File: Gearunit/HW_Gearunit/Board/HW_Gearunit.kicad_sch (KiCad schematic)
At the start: 37 parts, among them J1 XB-PJ-1837, J2 XB-PJ-1837, Q2 DMC2400UV, Q3 DMC2400UV, U11 LSM6DS3, U3 SIT1050TK, U4 AS5600-ASOT, U5 AS5600-ASOT, U6 CD4052B

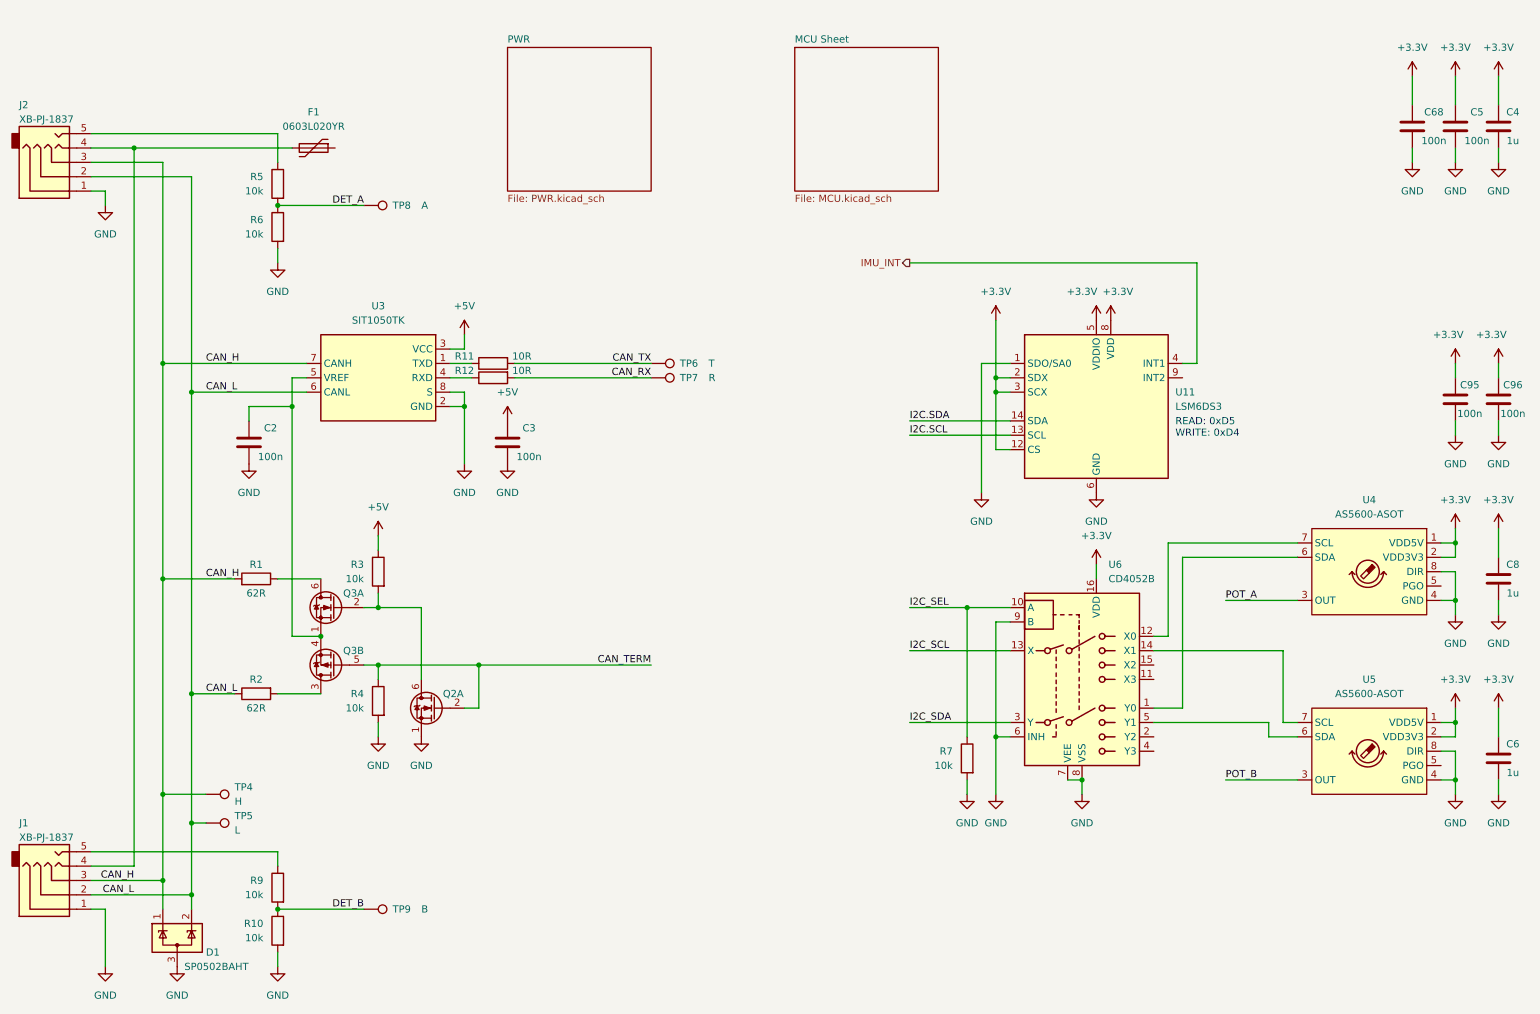
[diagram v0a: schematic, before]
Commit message: Gearunit updates, Readme updated
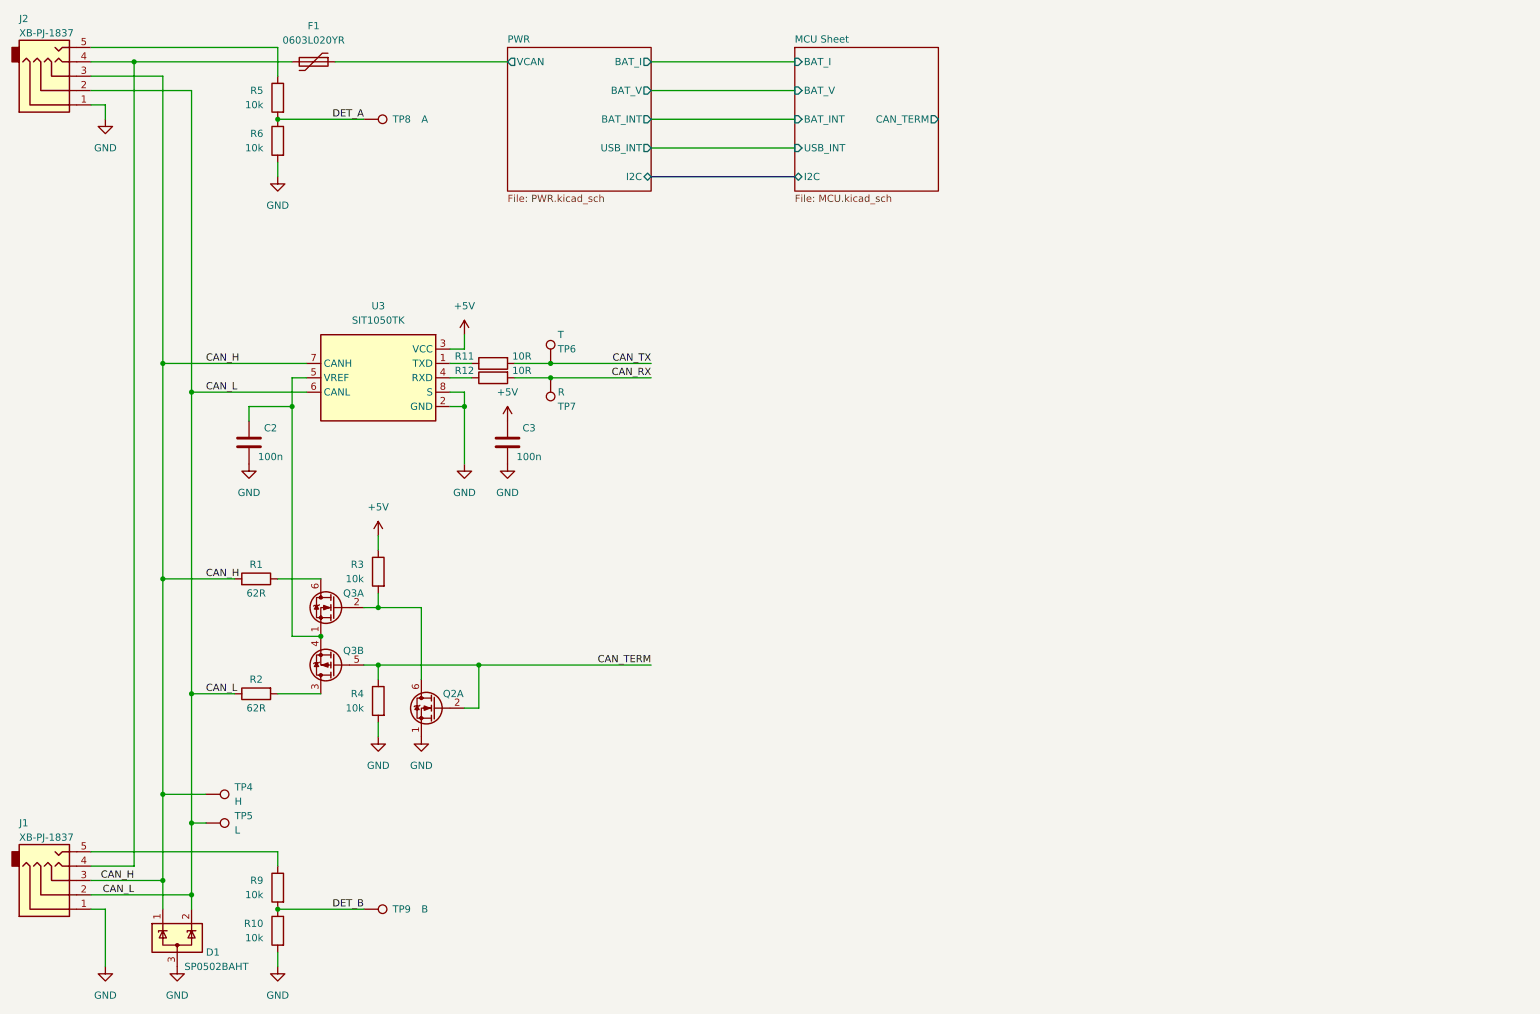
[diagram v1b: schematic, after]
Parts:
- removed C4, C6, C8: 1u, Capacitor_SMD:C_0603_1608Metric, symbol Device:C
- removed C5, C68, C95, C96: 100n, Capacitor_SMD:C_0402_1005Metric, symbol Device:C
- removed R7: 10k, Resistor_SMD:R_0402_1005Metric, symbol Device:R
- removed U11: LSM6DS3, Package_LGA:LGA-14_3x2.5mm_P0.5mm_LayoutBorder3x4y, symbol Sensor_Motion:LSM6DS3
- removed U4, U5: AS5600-ASOT, Package_SO:SO-8_3.9x4.9mm_P1.27mm, symbol USER:AS5600-ASOT
- removed U6: CD4052B, Package_SO:TSSOP-16_4.4x5mm_P0.65mm, symbol Analog_Switch:CD4052B
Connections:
- net PWR/VCAN: now reaches F1.1
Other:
- sheet MCU Sheet ports: added BAT_I, BAT_INT, BAT_V, CAN_TERM, I2C, USB_INT; removed none
- sheet PWR ports: added BAT_I, BAT_INT, BAT_V, I2C, USB_INT, VCAN; removed none
- note removed: "READ: 0xD5 WRITE: 0xD4"
- moved on the sheet: F1, J2, R5, R6, TP6, TP7, TP8
